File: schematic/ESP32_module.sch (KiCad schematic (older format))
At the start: 22 parts, among them J1 Conn_02x03_Odd_Even, J14 Conn_01x10_Male, J2 Conn_02x05_Odd_Even, J3 Conn_02x06_Odd_Even, U1 ESP32-WROOM-32

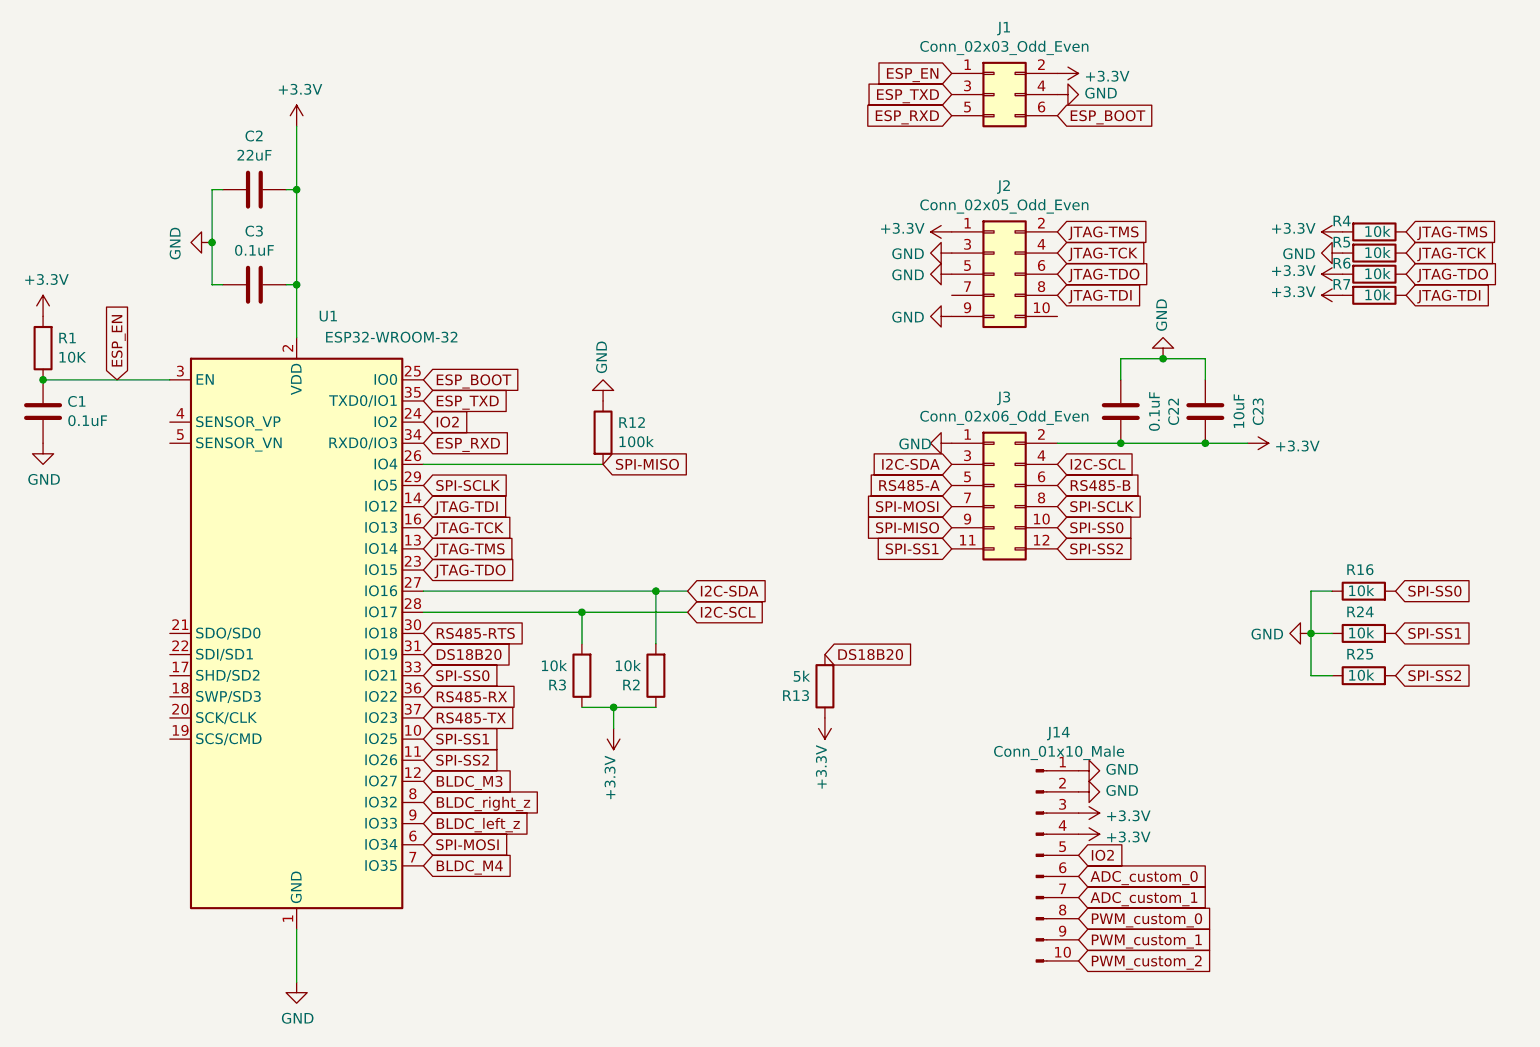
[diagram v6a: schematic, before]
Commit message: JTAG anti-ring resistors
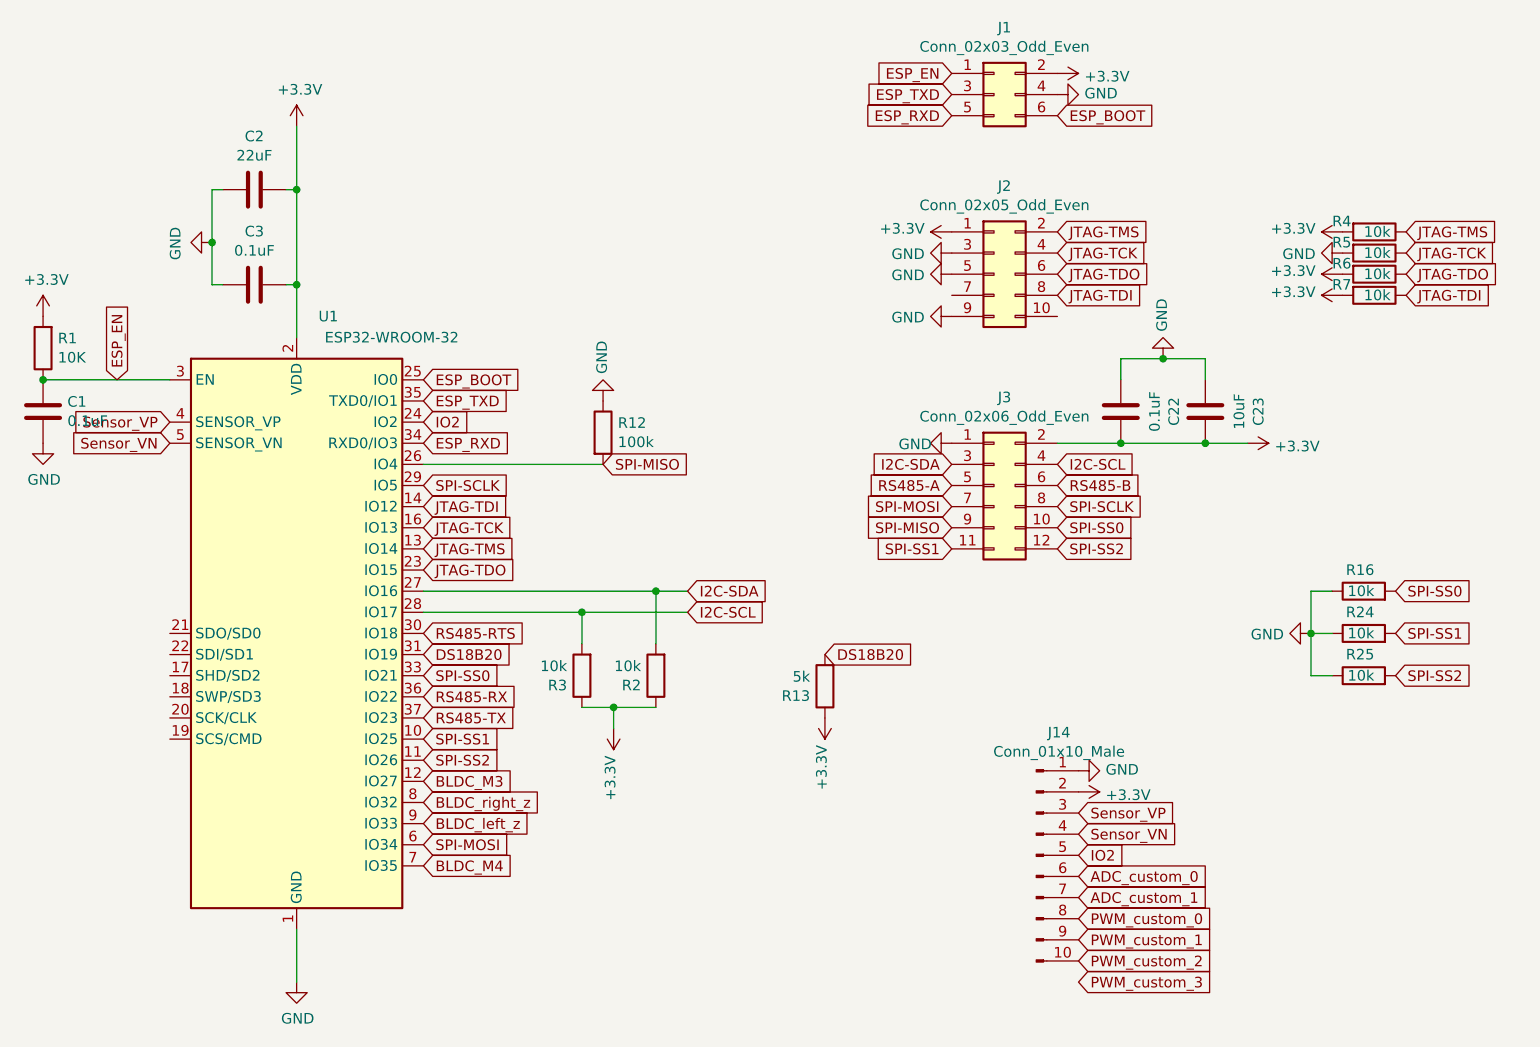
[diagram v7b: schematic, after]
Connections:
- net +3V3: now also J14.2 (Pin_2); no longer J14.3 (Pin_3), J14.4 (Pin_4)
- net GND: no longer J14.2 (Pin_2)
- net Sensor_VP: now reaches U1.4 (SENSOR_VP)
- net Sensor_VP: now also J14.3 (Pin_3)
- net Sensor_VN: now reaches U1.5 (SENSOR_VN)
- net Sensor_VN: now also J14.4 (Pin_4)
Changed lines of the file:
@@
 L power:+3.3V #PWR?
 U 1 1 5EFA72FF
-P 6250 5150
+P 6250 5050
 AR Path="/5EFA72FF" Ref="#PWR?"  Part="1"
 AR Path="/5ED629AF/5EFA72FF" Ref="#PWR0110"  Part="1"
-F 0 "#PWR0110" H 6250 5000 50  0001 C CNN
-F 1 "+3.3V" V 6265 5278 50  0000 L CNN
-F 2 "" H 6250 5150 50  0001 C CNN
-F 3 "" H 6250 5150 50  0001 C CNN
-	1    6250 5150
+F 0 "#PWR0110" H 6250 4900 50  0001 C CNN
+F 1 "+3.3V" V 6265 5178 50  0000 L CNN
+F 2 "" H 6250 5050 50  0001 C CNN
+F 3 "" H 6250 5050 50  0001 C CNN
+	1    6250 5050
 	0    1    1    0
 $EndComp
 Text GLabel 6250 5350 2    50   Input ~ 0
 IO2
-$Comp
-L power:+3.3V #PWR?
-U 1 1 5EFAB189
-P 6250 5250
-AR Path="/5EFAB189" Ref="#PWR?"  Part="1"
-AR Path="/5ED629AF/5EFAB189" Ref="#PWR0111"  Part="1"
-F 0 "#PWR0111" H 6250 5100 50  0001 C CNN
-F 1 "+3.3V" V 6265 5378 50  0000 L CNN
-F 2 "" H 6250 5250 50  0001 C CNN
-F 3 "" H 6250 5250 50  0001 C CNN
-	1    6250 5250
-	0    1    1    0
-$EndComp
-$Comp
-L power:GND #PWR?
-U 1 1 5EFAB62F
-P 6250 5050
-AR Path="/5EFAB62F" Ref="#PWR?"  Part="1"
-AR Path="/5ED629AF/5EFAB62F" Ref="#PWR0112"  Part="1"
-F 0 "#PWR0112" H 6250 4800 50  0001 C CNN
-F 1 "GND" V 6255 4922 50  0000 R CNN
-F 2 "" H 6250 5050 50  0001 C CNN
-F 3 "" H 6250 5050 50  0001 C CNN
-	1    6250 5050
-	0    -1   -1   0
-$EndComp
 Text GLabel 6250 5450 2    50   Input ~ 0
 ADC_custom_0
@@
 Wire Wire Line
 	6650 3000 6850 3000
+Text GLabel 1950 3300 0    50   Input ~ 0
+Sensor_VP
+Text GLabel 6250 5150 2    50   Input ~ 0
+Sensor_VP
+Text GLabel 1950 3400 0    50   Input ~ 0
+Sensor_VN
+Text GLabel 6250 5250 2    50   Input ~ 0
+Sensor_VN
+Text GLabel 6250 5950 2    50   Input ~ 0
+PWM_custom_3
 $EndSCHEMATC

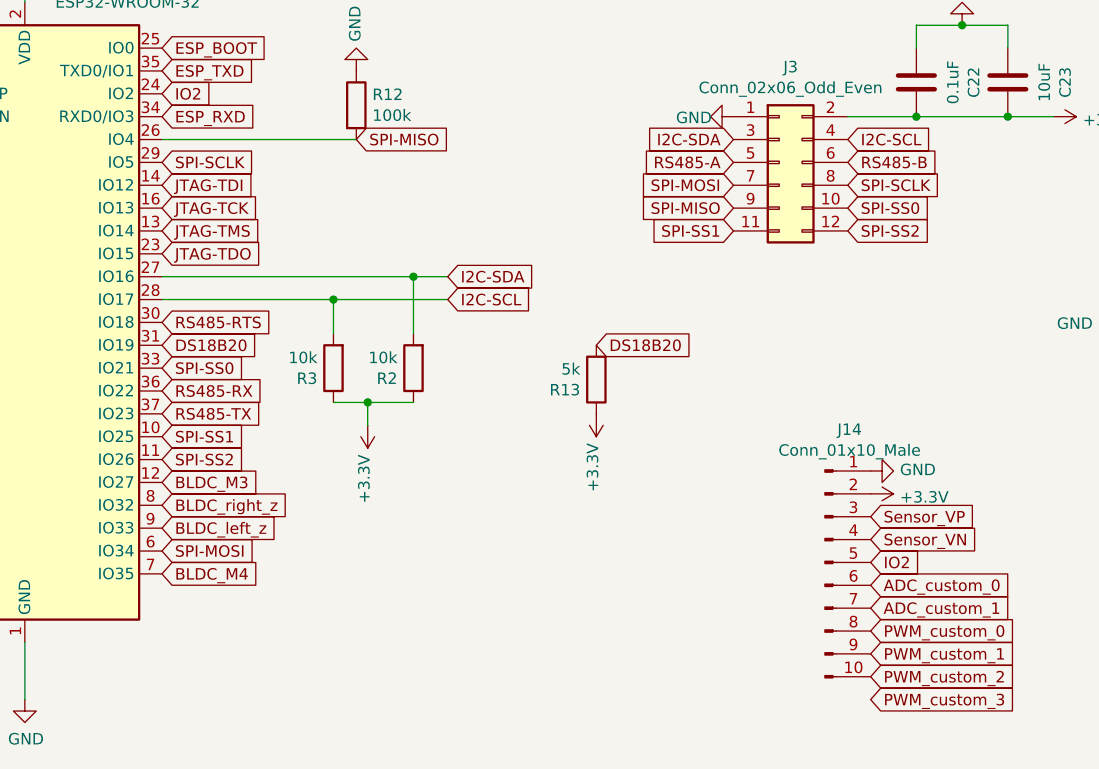
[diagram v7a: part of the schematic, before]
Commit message: adjusted 1.27mm IDC and PCA9685 to correct footprint
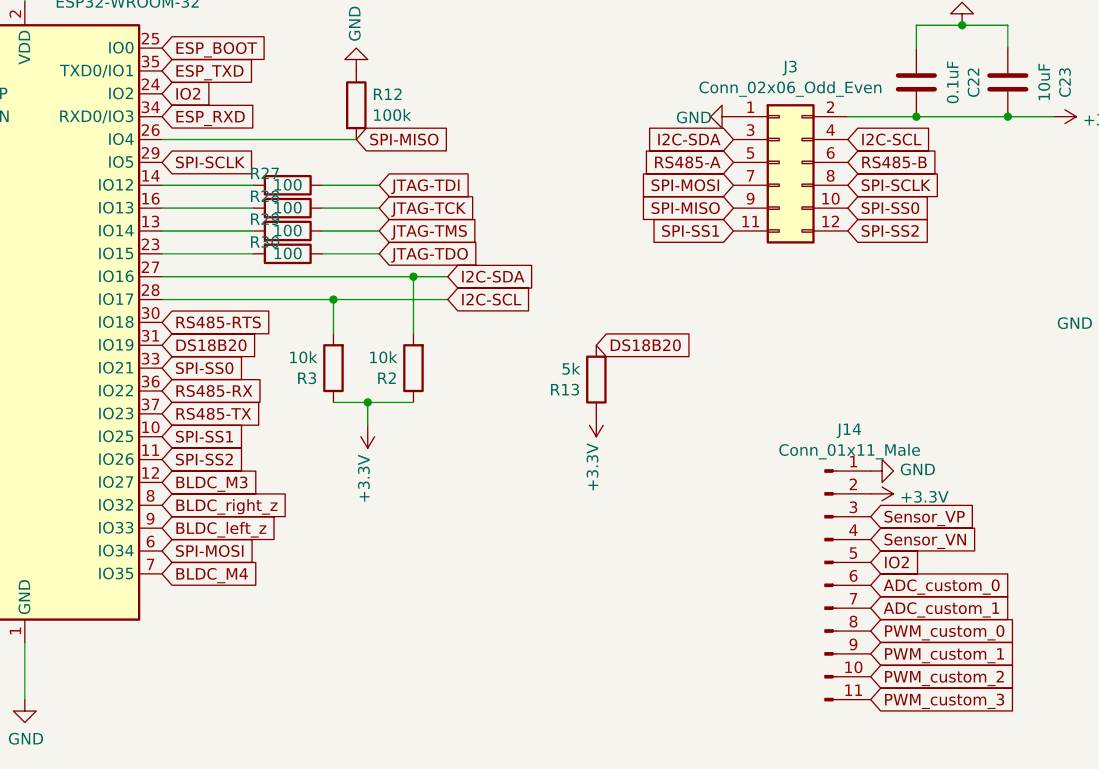
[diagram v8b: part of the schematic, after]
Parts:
- removed J14: Conn_01x10_Male, Connector_PinHeader_2.54mm:PinHeader_1x10_P2.54mm_Vertical, symbol Connector:Conn_01x10_Male
- added J14: Conn_01x11_Male, Connector_PinHeader_2.54mm:PinHeader_1x11_P2.54mm_Vertical, symbol Connector:Conn_01x11_Male
- added R27, R28, R29, R30: 100, Resistor_SMD:R_0805_2012Metric_Pad1.15x1.40mm_HandSolder, symbol Device:R
- J2: footprint Connector_PinHeader_1.27mm:PinHeader_2x05_P1.27mm_Vertical_SMD -> Apsu:10pin1.27mmIDC
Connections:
- net +3V3: now also J14.2 (Pin_2)
- net ADC_custom_0: now also J14.6 (Pin_6)
- net ADC_custom_1: now also J14.7 (Pin_7)
- net GND: now also J14.1 (Pin_1)
- net IO2: now also J14.5 (Pin_5)
- net JTAG-TCK: now also R28.1; no longer U1.16 (IO13)
- net JTAG-TDI: now also R27.1; no longer U1.14 (IO12)
- net JTAG-TDO: now also R30.1; no longer U1.23 (IO15)
- net JTAG-TMS: now also R29.1; no longer U1.13 (IO14)
- net PWM_custom_0: now also J14.8 (Pin_8)
- net PWM_custom_1: now also J14.9 (Pin_9)
- net PWM_custom_2: now also J14.10 (Pin_10)
- net PWM_custom_3: now also J14.11 (Pin_11)
- net Sensor_VN: now also J14.4 (Pin_4)
- net Sensor_VP: now also J14.3 (Pin_3)
- new net: R29.2, U1.13 (IO14)
- new net: R27.2, U1.14 (IO12)
- new net: R28.2, U1.16 (IO13)
- new net: R30.2, U1.23 (IO15)
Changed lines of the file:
@@
 	1    0    0    -1
 $EndComp
-Text GLabel 3150 4000 2    50   Input ~ 0
+Text GLabel 4100 4000 2    50   Input ~ 0
 JTAG-TDO
-Text GLabel 3150 3700 2    50   Input ~ 0
+Text GLabel 4100 3700 2    50   Input ~ 0
 JTAG-TDI
-Text GLabel 3150 3800 2    50   Input ~ 0
+Text GLabel 4100 3800 2    50   Input ~ 0
 JTAG-TCK
-Text GLabel 3150 3900 2    50   Input ~ 0
+Text GLabel 4100 3900 2    50   Input ~ 0
 JTAG-TMS
 $Comp
@@
 F 0 "J2" H 5900 3017 50  0000 C CNN
 F 1 "Conn_02x05_Odd_Even" H 5900 2926 50  0000 C CNN
-F 2 "Connector_PinHeader_1.27mm:PinHeader_2x05_P1.27mm_Vertical_SMD" H 5850 2600 50  0001 C CNN
+F 2 "Apsu:10pin1.27mmIDC" H 5850 2600 50  0001 C CNN
 F 3 "~" H 5850 2600 50  0001 C CNN
 	1    5850 2600
@@
 Wire Wire Line
 	7450 4300 7350 4300
-$Comp
-L Connector:Conn_01x10_Male J14
-U 1 1 5EFA3108
-P 6050 5350
-F 0 "J14" H 6158 5931 50  0000 C CNN
-F 1 "Conn_01x10_Male" H 6158 5840 50  0000 C CNN
-F 2 "Connector_PinHeader_2.54mm:PinHeader_1x10_P2.54mm_Vertical" H 6050 5350 50  0001 C CNN
-F 3 "~" H 6050 5350 50  0001 C CNN
-	1    6050 5350
-	1    0    0    -1
-$EndComp
 Text GLabel 3150 3300 2    50   Input ~ 0
 IO2
@@
 Text GLabel 6250 5950 2    50   Input ~ 0
 PWM_custom_3
+$Comp
+L Device:R R27
+U 1 1 5F00381B
+P 3700 3700
+F 0 "R27" V 3650 3600 50  0000 C CNN
+F 1 "100" V 3700 3700 50  0000 C CNN
+F 2 "Resistor_SMD:R_0805_2012Metric_Pad1.15x1.40mm_HandSolder" V 3630 3700 50  0001 C CNN
+F 3 "~" H 3700 3700 50  0001 C CNN
+	1    3700 3700
+	0    1    1    0
+$EndComp
+$Comp
+L Device:R R28
+U 1 1 5F009BC7
+P 3700 3800
+F 0 "R28" V 3650 3700 50  0000 C CNN
+F 1 "100" V 3700 3800 50  0000 C CNN
+F 2 "Resistor_SMD:R_0805_2012Metric_Pad1.15x1.40mm_HandSolder" V 3630 3800 50  0001 C CNN
+F 3 "~" H 3700 3800 50  0001 C CNN
+	1    3700 3800
+	0    1    1    0
+$EndComp
+$Comp
+L Device:R R29
+U 1 1 5F009E9D
+P 3700 3900
+F 0 "R29" V 3650 3800 50  0000 C CNN
+F 1 "100" V 3700 3900 50  0000 C CNN
+F 2 "Resistor_SMD:R_0805_2012Metric_Pad1.15x1.40mm_HandSolder" V 3630 3900 50  0001 C CNN
+F 3 "~" H 3700 3900 50  0001 C CNN
+	1    3700 3900
+	0    1    1    0
+$EndComp
+$Comp
+L Device:R R30
+U 1 1 5F00A19D
+P 3700 4000
+F 0 "R30" V 3650 3900 50  0000 C CNN
+F 1 "100" V 3700 4000 50  0000 C CNN
+F 2 "Resistor_SMD:R_0805_2012Metric_Pad1.15x1.40mm_HandSolder" V 3630 4000 50  0001 C CNN
+F 3 "~" H 3700 4000 50  0001 C CNN
+	1    3700 4000
+	0    1    1    0
+$EndComp
+Wire Wire Line
+	3150 3700 3550 3700
+Wire Wire Line
+	3150 3800 3550 3800
+Wire Wire Line
+	3150 3900 3550 3900
+Wire Wire Line
+	3150 4000 3550 4000
+Wire Wire Line
+	3850 3700 4100 3700
+Wire Wire Line
+	3850 3800 4100 3800
+Wire Wire Line
+	3850 3900 4100 3900
+Wire Wire Line
+	3850 4000 4100 4000
+$Comp
+L Connector:Conn_01x11_Male J14
+U 1 1 5F020876
+P 6050 5450
+F 0 "J14" H 6158 6131 50  0000 C CNN
+F 1 "Conn_01x11_Male" H 6158 6040 50  0000 C CNN
+F 2 "Connector_PinHeader_2.54mm:PinHeader_1x11_P2.54mm_Vertical" H 6050 5450 50  0001 C CNN
+F 3 "~" H 6050 5450 50  0001 C CNN
+	1    6050 5450
+	1    0    0    -1
+$EndComp
 $EndSCHEMATC
